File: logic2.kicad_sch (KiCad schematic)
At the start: 22 parts, among them U12 IN74ALS02N (КР1533ЛЕ1), U21 SN74ALS14 (КР1533ТЛ2), U29 IN74ALS32N (КР1533ЛЛ1), U30 IN74ALS02N (КР1533ЛЕ1), U40 IN74ALS00N (КР1533ЛА3), U49 SN74ALS04 (КР1533ЛН1), U52 SN74ALS175N (КР1533ТМ8), U54 SN74ALS298N (КР1533КП13), U56 SN74ALS175N (КР1533ТМ8), U59 SN74ALS175N (КР1533ТМ8), U61 SN74ALS298N (КР1533КП13), U63 SN74ALS175N (КР1533ТМ8)

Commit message: 20 march version
Added 2nd list, working on the third
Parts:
- removed unit 2 of U12
- added D11, D12, D13: 1N4148 (КД522Б), symbol Device:D
- added R32, R35, R36, R39: 470, symbol Device:R
- added R34, R38, R41: 2.7K, symbol Device:R
- added R37: 1.5K, symbol Device:R
- added R40: 5.6K, symbol Device:R
- added R45, R46: 1K, symbol Device:R
- added U14, U50: SN74ALS86N (КР1533ЛП5), Package_DIP:DIP-14_W7.62mm_Socket_LongPads, symbol 74xx:74LS86
- added U15: CD4520АN_(К561ИЕ10), Package_DIP:DIP-16_W7.62mm_Socket_LongPads, symbol w_connectors:CD4520АN_(К561ИЕ10)
- added unit 2 of U40
- added U51: SN7486N (К155ЛП5), Package_DIP:DIP-14_W7.62mm_Socket_LongPads, symbol 74xx:74LS86
- added U53, U60: SN74ALS153N (КР1533КП2), Package_DIP:DIP-16_W7.62mm_Socket_LongPads, symbol w_connectors:SN74ALS153N_(КР1533КП2)
- added U55, U62: 74LS257 (КР1533КП11А), Package_DIP:DIP-16_W7.62mm_Socket_LongPads, symbol 74xx:74LS257
- added U57, U58, U64, U65: SN74LS295N_(К555ИР16), Package_DIP:DIP-14_W7.62mm_Socket_LongPads, symbol w_connectors:SN74LS295N_(К555ИР16)
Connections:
- net +5V: now also R45.2, R46.2, U15.2 (Enable), U53.16 (VCC), U55.16 (VCC), U57.14 (VCC), U57.6 (Pe), U57.8 (OE), U58.14 (VCC), U58.8 (OE), U60.16 (VCC), U62.16 (VCC), U64.14 (VCC), U64.6 (Pe), U64.8 (OE), U65.14 (VCC), U65.8 (OE)
- net 7MHZ: now also U58.9 (Cp), U65.9 (Cp)
- net BD0: now also U62.14 (I0c), U64.2 (P0)
- net BD1: now also U62.2 (I0a), U64.3 (P1)
- net BD2: now also U62.5 (I0b), U64.4 (P2)
- net BD3: now also U55.2 (I0a), U64.5 (P3)
- net BD4: now also U57.2 (P0), U62.11 (I0d)
- net BD5: now also U55.5 (I0b), U57.3 (P1)
- net BD6: now also U55.11 (I0d), U57.4 (P2)
- net BD7: now also U55.14 (I0c), U57.5 (P3)
- net CHTRGL: now also U55.15 (OE), U62.15 (OE)
- net D0: now also U62.12 (Zc)
- net D1: now also U62.4 (Za)
- net D2: now also U62.7 (Zb)
- net D3: now also U55.4 (Za)
- net D4: now also U62.9 (Zd)
- net GND: now also U15.7 (Reset), U53.12 (I2b), U53.13 (I3b), U53.8 (GND), U55.8 (GND), U57.7 (GND), U58.7 (GND), U60.8 (GND), U62.8 (GND), U64.7 (GND), U65.1 (Ds), U65.7 (GND)
- net MAG: now also U55.10 (I1d)
- net VIBOZUL: now also U55.1 (S), U62.1 (S)
- net ZPVDN: now also U58.6 (Pe), U65.6 (Pe)
- net at U54.12 (Qd), U54.7 (I0d): now also U53.5 (I1a)
- net at U54.13 (Qc), U54.9 (I0c): now also U53.10 (I0b), U53.11 (I1b)
- net at U54.14 (Qb), U54.4 (I0b): now also U40.4
- net at U54.15 (Qa), U54.3 (I0a): now also U60.11 (I1b)
- net at U61.12 (Qd), U61.7 (I0d): now also U60.10 (I0b)
- net at U61.13 (Qc), U61.9 (I0c): now also U53.6 (I0a)
- net at U61.14 (Qb), U61.4 (I0b): now also U60.5 (I1a)
- net at U61.15 (Qa), U61.3 (I0a): now also U60.6 (I0a)
- net at U52.10 (Q2): now also U60.12 (I2b), U60.13 (I3b)
- net at U52.15 (Q3): now also U53.3 (I3a), U53.4 (I2a)
- net at U52.2 (Q0): now also U60.3 (I3a), U60.4 (I2a)
- net at U49.12: now also U51.2
- net at U49.13: now also U14.3
- new net: R32.1, U51.6
- new net: D13.1 (K), R41.2
- new net: U58.1 (Ds), U65.10 (Q3)
- new net: U64.13 (Q0), U65.2 (P0)
- new net: U64.12 (Q1), U65.3 (P1)
- new net: U64.11 (Q2), U65.4 (P2)
- new net: U64.10 (Q3), U65.5 (P3)
- new net: R45.1, R46.1, U51.1, U51.10, U51.13, U51.5
- new net: R34.1, R38.1, R41.1, U53.9 (Zb)
- new net: D12.1 (K), R38.2
- new net: R39.1, U51.11
- new net: R35.1, U51.3
- new net: R36.1, U51.8
- new net: U51.9, U60.7 (Za)
- new net: U15.6 (Q4), U40.5
- new net: U40.6, U50.9
- new net: U50.8, U60.14 (S0)
- new net: U51.4, U60.9 (Zb)
- new net: U51.12, U53.7 (Za)
- new net: D11.1 (K), R34.2
- new net: U57.10 (Q3), U58.5 (P3)
- new net: U57.11 (Q2), U58.4 (P2)
- new net: U57.12 (Q1), U58.3 (P1)
- new net: U57.13 (Q0), U58.2 (P0)
- new net: U50.10, U58.10 (Q3)
- new net CCML: U14.2
- new net D5: U55.7 (Zb)
- new net D6: U55.9 (Zd)
- new net D7: U55.12 (Zc)
- new net KB0: U62.13 (I1c)
- new net KB1: U62.3 (I1a)
- new net KB2: U62.6 (I1b)
- new net KB3: U55.3 (I1a)
- new net KB4: U62.10 (I1d)
- new net KB5: U55.6 (I1b)
- new net KB7: U55.13 (I1c)
- new net KRAIN: U53.2 (S1), U60.2 (S1)
- new net KSGIN: U53.1 (Ea), U53.15 (Eb), U60.1 (Ea), U60.15 (Eb)
- new net SYNCRO: R35.2
- new net TAIML: U14.1
- new net TAIMS: U15.1 (CK)
- new net YB: D13.2 (A), R39.2
- new net YG: D11.2 (A), R32.2
- new net YR: D12.2 (A), R36.2
- new net ZPRGBD: U57.9 (Cp), U64.9 (Cp)
- no-connect marks 22 -> 33
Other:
- moved on the sheet: C10, C11, C14, D30, D31, J?, R11, R12, R20, R21, U12A, U12C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

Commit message: March 21st update
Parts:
- removed unit 3 of U14
- removed unit 2 of U14
- removed unit 2 of U49

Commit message: March 22nd additions
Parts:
- removed unit 4 of U14
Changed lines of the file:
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@@
     (pin "1")
-  )
-  (symbol (lib_id "74xx:74LS86") (at 1031.875 120.65 0) (unit 4)
-    (in_bom yes) (on_board yes) (fields_autoplaced)
-    (property "Reference" "U14" (id 0) (at 1031.5702 111.125 0))
-    (property "Value" "SN74ALS86N (КР1533ЛП5)" (id 1) (at 1031.5702 113.665 0))
-    (property "Footprint" "Package_DIP:DIP-14_W7.62mm_Socket_LongPads" (id 2) (at 1031.875 120.65 0)
-      (effects (font (size 1.27 1.27)) hide)
-    )
-    (property "Datasheet" "74xx/74ls86.pdf" (id 3) (at 1031.875 120.65 0)
-      (effects (font (size 1.27 1.27)) hide)
-    )
-    (pin "1")
-    (pin "2")
-    (pin "3")
-    (pin "4")
-    (pin "5")
-    (pin "6")
-    (pin "10")
-    (pin "8")
-    (pin "9")
-    (pin "11")
-    (pin "12")
-    (pin "13")
-    (pin "14")
-    (pin "7")
   )
   (symbol (lib_id "74xx:74LS86") (at 328.295 130.175 0) (mirror x) (unit 1)

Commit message: March 22nd - 3rd edition
List 3 is complete
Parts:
- gave numbers to parts that had none: 1
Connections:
- net TAIML is gone; now on net TAIMS: U14.1
- net +5V: now also U12.14 (VCC), U14.14 (VCC), U15.16 (VDD), U29.14 (VCC), U30.14 (VCC), U49.14 (VCC), U50.14 (VCC), U51.14 (VCC)
- net GND: now also U12.7 (GND), U14.7 (GND), U15.8 (VSS), U29.7 (GND), U30.7 (GND), U49.7 (GND), U50.7 (GND), U51.7 (GND)
- net at U50.8, U60.14 (S0): now also U53.14 (S0)
- no-connect marks 33 -> 61
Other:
- moved on the sheet: U14E

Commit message: March 23rd Update 1
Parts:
- removed R37: 1.5K, symbol Device:R
- removed R40: 5.6K, symbol Device:R
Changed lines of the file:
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@@
     (pin "1")
-  )
-  (symbol (lib_id "Device:R") (at 1038.225 210.185 90) (unit 1)
-    (in_bom yes) (on_board yes)
-    (property "Reference" "R40" (id 0) (at 1038.225 207.645 90))
-    (property "Value" "5.6K" (id 1) (at 1038.225 210.185 90))
-    (property "Footprint" "" (id 2) (at 1038.225 211.963 90)
-      (effects (font (size 1.27 1.27)) hide)
-    )
-    (property "Datasheet" "~" (id 3) (at 1038.225 210.185 0)
-      (effects (font (size 1.27 1.27)) hide)
-    )
-    (pin "1")
-    (pin "2")
   )
   (symbol (lib_id "w_connectors:CD4520АN_(К561ИЕ10)") (at 899.795 126.365 0) (unit 3)
@@
     (pin "7")
   )
-  (symbol (lib_id "Device:R") (at 1037.59 198.755 90) (unit 1)
-    (in_bom yes) (on_board yes)
-    (property "Reference" "R37" (id 0) (at 1037.59 196.215 90))
-    (property "Value" "1.5K" (id 1) (at 1037.59 198.755 90))
-    (property "Footprint" "" (id 2) (at 1037.59 200.533 90)
-      (effects (font (size 1.27 1.27)) hide)
-    )
-    (property "Datasheet" "~" (id 3) (at 1037.59 198.755 0)
-      (effects (font (size 1.27 1.27)) hide)
-    )
-    (pin "1")
-    (pin "2")
-  )
   (symbol (lib_id "74xx:74LS86") (at 995.68 188.595 0) (unit 1)

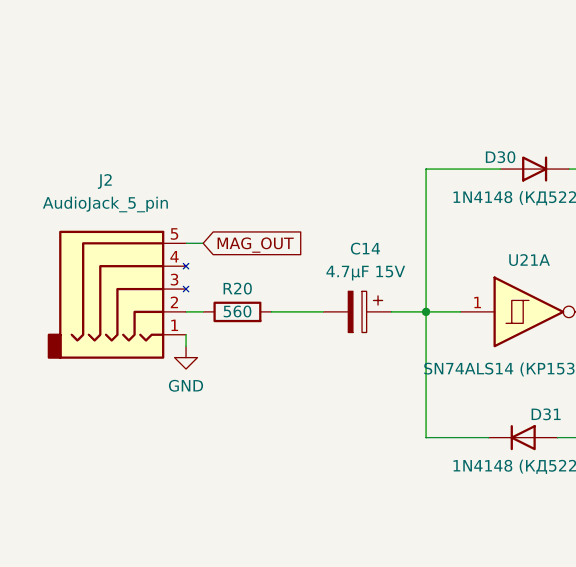
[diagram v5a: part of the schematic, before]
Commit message: March 23rd First pre-alpha
First time ZERO errors and 93 warnings. Schematics are done, now to deal with warnings and footprints.
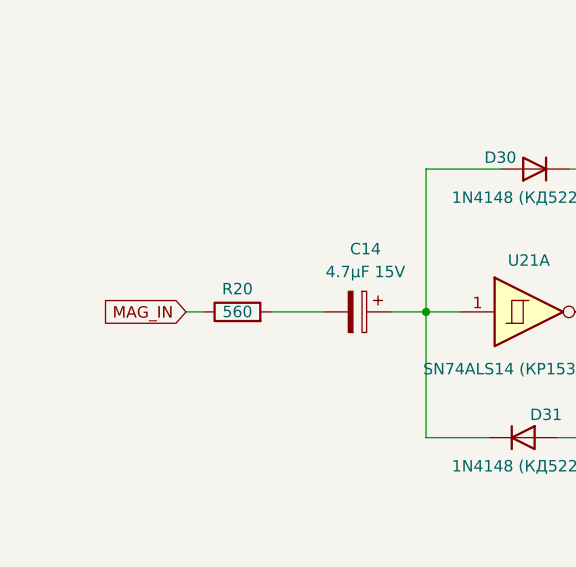
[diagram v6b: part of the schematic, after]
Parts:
- removed J2: AudioJack_5_pin, symbol w_connectors:AudioJack_5_pin
- C10, C11: footprint (none) -> Capacitor_THT:C_Disc_D7.0mm_W2.5mm_P5.00mm
- C14: footprint (none) -> Capacitor_THT:CP_Radial_D10.0mm_P5.00mm
- D11, D12, D13, D30, D31: footprint (none) -> Diode_THT:D_DO-35_SOD27_P10.16mm_Horizontal
- R11, R12, R20, R21, R32, R34, R35, R36, R38, R39, R41, R45, R46: footprint (none) -> Resistor_THT:R_Axial_DIN0207_L6.3mm_D2.5mm_P10.16mm_Horizontal
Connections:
- net MAG_IN: now reaches R20.1

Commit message: March 24th - First Edition of PCB
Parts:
- removed U56, U63: SN74ALS175N (КР1533ТМ8), Package_DIP:DIP-16_W7.62mm_Socket_LongPads, symbol w_connectors:SN74ALS175N
- added U56: SN74ALS175N_U56, Package_DIP:DIP-16_W7.62mm_Socket_LongPads, symbol w_connectors:SN74ALS175N_U56
- added U63: SN74ALS175N_U63, Package_DIP:DIP-16_W7.62mm_Socket_LongPads, symbol w_connectors:SN74ALS175N_U63
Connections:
- net +5V: now also U56.1 (~{Mr}), U56.16 (VCC), U63.1 (~{Mr}), U63.16 (VCC)
- net BD0: now also U63.4 (D0)
- net BD1: now also U63.5 (D1)
- net BD2: now also U63.12 (D2)
- net BD3: now also U63.13 (D3)
- net BD4: now also U56.4 (D0)
- net BD5: now also U56.5 (D1)
- net BD6: now also U56.12 (D2)
- net BD7: now also U56.13 (D3)
- net GND: now also U56.8 (GND), U63.8 (GND)
- net ZPRGAT+: now also U56.9 (Cp), U63.9 (Cp)
- net at U54.1 (I1b): now also U56.10 (Q2)
- net at U54.2 (I1a): now also U56.2 (Q0)
- net at U54.5 (I1c): now also U56.15 (Q3)
- net at U54.6 (I1d): now also U56.7 (Q1)
- net at U61.1 (I1b): now also U63.15 (Q3)
- net at U61.2 (I1a): now also U63.2 (Q0)
- net at U61.5 (I1c): now also U63.10 (Q2)
- net at U61.6 (I1d): now also U63.7 (Q1)
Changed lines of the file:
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@@
     (pin "1")
-  )
-  (symbol (lib_name "SN74ALS175N_2") (lib_id "w_connectors:SN74ALS175N") (at 180.975 99.695 0) (unit 1)
-    (in_bom yes) (on_board yes) (fields_autoplaced)
-    (property "Reference" "U56" (id 0) (at 182.9944 81.28 0)
-      (effects (font (size 1.27 1.27)) (justify left))
-    )
-    (property "Value" "SN74ALS175N (КР1533ТМ8)" (id 1) (at 182.9944 83.82 0)
-      (effects (font (size 1.27 1.27)) (justify left))
-    )
-    (property "Footprint" "Package_DIP:DIP-16_W7.62mm_Socket_LongPads" (id 2) (at 180.975 121.285 0)
-      (effects (font (size 1.27 1.27)) hide)
-    )
-    (property "Datasheet" "http://www.ti.com/lit/gpn/sn74LS175" (id 3) (at 180.975 75.565 0)
-      (effects (font (size 1.27 1.27)) hide)
-    )
-    (pin "1")
-    (pin "10")
-    (pin "11")
-    (pin "12")
-    (pin "13")
-    (pin "14")
-    (pin "15")
-    (pin "16")
-    (pin "2")
-    (pin "3")
-    (pin "4")
-    (pin "5")
-    (pin "6")
-    (pin "7")
-    (pin "8")
-    (pin "9")
   )
   (symbol (lib_id "Device:R") (at 347.345 64.77 90) (unit 1)
@@
     (pin "7")
   )
+  (symbol (lib_id "w_connectors:SN74ALS175N_U63") (at 180.975 49.53 0) (unit 1)
+    (in_bom yes) (on_board yes) (fields_autoplaced)
+    (property "Reference" "U63" (id 0) (at 182.9944 32.385 0)
+      (effects (font (size 1.27 1.27)) (justify left))
+    )
+    (property "Value" "SN74ALS175N_U63" (id 1) (at 182.9944 34.925 0)
+      (effects (font (size 1.27 1.27)) (justify left))
+    )
+    (property "Footprint" "Package_DIP:DIP-16_W7.62mm_Socket_LongPads" (id 2) (at 180.975 71.12 0)
+      (effects (font (size 1.27 1.27)) hide)
+    )
+    (property "Datasheet" "http://www.ti.com/lit/gpn/sn74LS175" (id 3) (at 180.975 25.4 0)
+      (effects (font (size 1.27 1.27)) hide)
+    )
+    (pin "1")
+    (pin "10")
+    (pin "11")
+    (pin "12")
+    (pin "13")
+    (pin "14")
+    (pin "15")
+    (pin "16")
+    (pin "2")
+    (pin "3")
+    (pin "4")
+    (pin "5")
+    (pin "6")
+    (pin "7")
+    (pin "8")
+    (pin "9")
+  )
   (symbol (lib_name "74LS298_1") (lib_id "74xx:74LS298") (at 237.49 48.26 0) (unit 1)
     (in_bom yes) (on_board yes) (fields_autoplaced)
@@
     (pin "7")
   )
-  (symbol (lib_name "SN74ALS175N_1") (lib_id "w_connectors:SN74ALS175N") (at 180.975 49.53 0) (unit 1)
-    (in_bom yes) (on_board yes)
-    (property "Reference" "U63" (id 0) (at 182.9944 31.115 0)
-      (effects (font (size 1.27 1.27)) (justify left))
-    )
-    (property "Value" "SN74ALS175N (КР1533ТМ8)" (id 1) (at 167.64 24.765 0)
-      (effects (font (size 1.27 1.27)) (justify left))
-    )
-    (property "Footprint" "Package_DIP:DIP-16_W7.62mm_Socket_LongPads" (id 2) (at 180.975 71.12 0)
-      (effects (font (size 1.27 1.27)) hide)
-    )
-    (property "Datasheet" "http://www.ti.com/lit/gpn/sn74LS175" (id 3) (at 180.975 25.4 0)
-      (effects (font (size 1.27 1.27)) hide)
-    )
-    (pin "1")
-    (pin "10")
-    (pin "11")
-    (pin "12")
-    (pin "13")
-    (pin "14")
-    (pin "15")
-    (pin "16")
-    (pin "2")
-    (pin "3")
-    (pin "4")
-    (pin "5")
-    (pin "6")
-    (pin "7")
-    (pin "8")
-    (pin "9")
-  )
   (symbol (lib_id "74xx:74LS02") (at 108.585 198.12 0) (mirror x) (unit 4)
     (in_bom yes) (on_board yes)
@@
     (pin "1")
   )
+  (symbol (lib_id "w_connectors:SN74ALS175N_U56") (at 180.975 99.695 0) (unit 1)
+    (in_bom yes) (on_board yes) (fields_autoplaced)
+    (property "Reference" "U56" (id 0) (at 182.9944 81.28 0)
+      (effects (font (size 1.27 1.27)) (justify left))
+    )
+    (property "Value" "SN74ALS175N_U56" (id 1) (at 182.9944 83.82 0)
+      (effects (font (size 1.27 1.27)) (justify left))
+    )
+    (property "Footprint" "Package_DIP:DIP-16_W7.62mm_Socket_LongPads" (id 2) (at 180.975 121.285 0)
+      (effects (font (size 1.27 1.27)) hide)
+    )
+    (property "Datasheet" "http://www.ti.com/lit/gpn/sn74LS175" (id 3) (at 180.975 75.565 0)
+      (effects (font (size 1.27 1.27)) hide)
+    )
+    (pin "1")
+    (pin "10")
+    (pin "11")
+    (pin "12")
+    (pin "13")
+    (pin "14")
+    (pin "15")
+    (pin "16")
+    (pin "2")
+    (pin "3")
+    (pin "4")
+    (pin "5")
+    (pin "6")
+    (pin "7")
+    (pin "8")
+    (pin "9")
+  )
   (symbol (lib_id "74xx:74LS00") (at 260.35 151.13 0) (unit 2)
     (in_bom yes) (on_board yes)
@@
     (pin "9")
   )
-  (symbol (lib_id "w_connectors:SN74ALS175N") (at 114.935 93.345 0) (unit 1)
+  (symbol (lib_name "SN74ALS175N_3") (lib_id "w_connectors:SN74ALS175N") (at 114.935 93.345 0) (unit 1)
     (in_bom yes) (on_board yes) (fields_autoplaced)
     (property "Reference" "U59" (id 0) (at 116.9544 74.93 0)
